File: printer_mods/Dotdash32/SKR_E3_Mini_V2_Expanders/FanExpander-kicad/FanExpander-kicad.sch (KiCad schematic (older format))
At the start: 66 parts, among them J0 FAN0, J1 FAN1, J10 FAN0_IN, J11 HI_PWR_Inputs, J2 FAN2, J3 FAN3, J4 FAN4, J5 FAN5, J6 FAN6, J7 FAN7, J8 EXP1_IN, J9 5V_In, Q1 IRLML6344, Q2 IRLML6344, Q3 IRLML6344, Q4 IRLML6344, Q5 IRLML6344, Q6 IRLML6344, Q7 IRLML6344

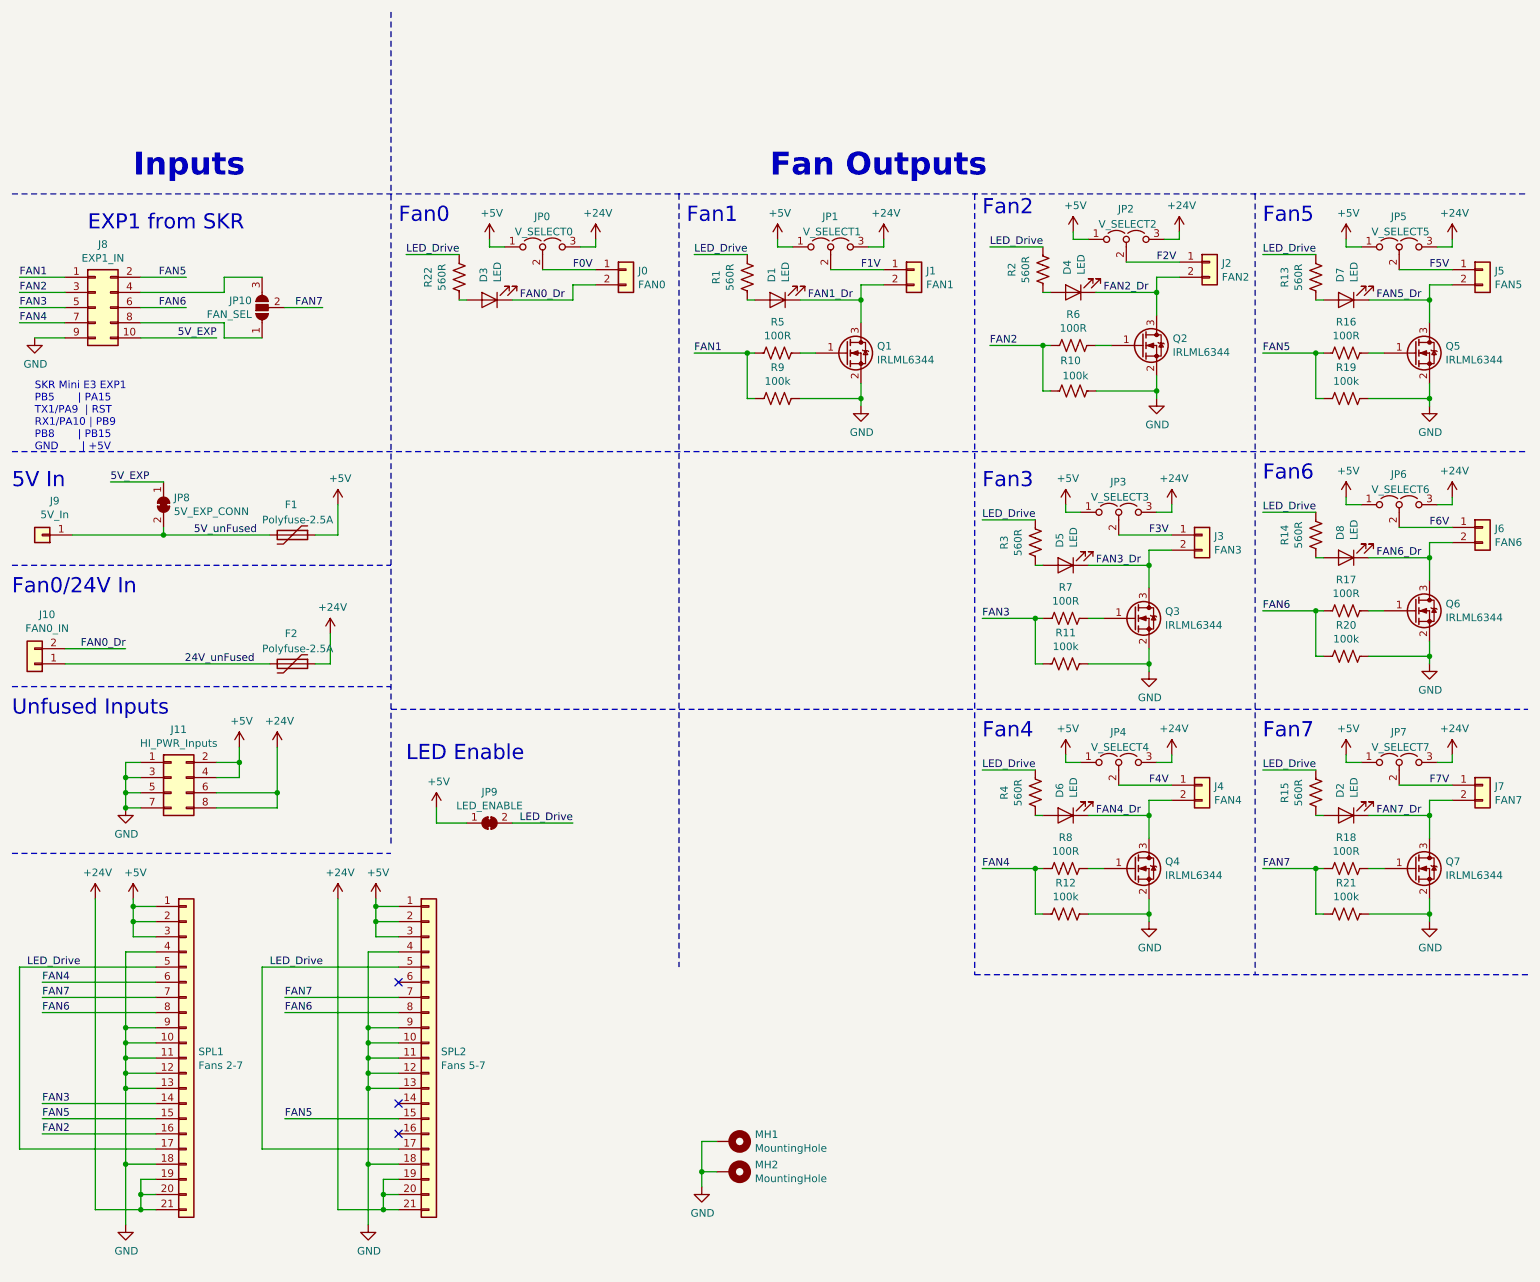
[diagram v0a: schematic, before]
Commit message: feat: move SMD components to bottom for sizing
this really messes with the designator cleanliness, but alas,
sacrifices must be made.  It's really smalll now!

Also some schematic cleaning.  Should there be a second set of
mounting holes next to the connector?  unclear...
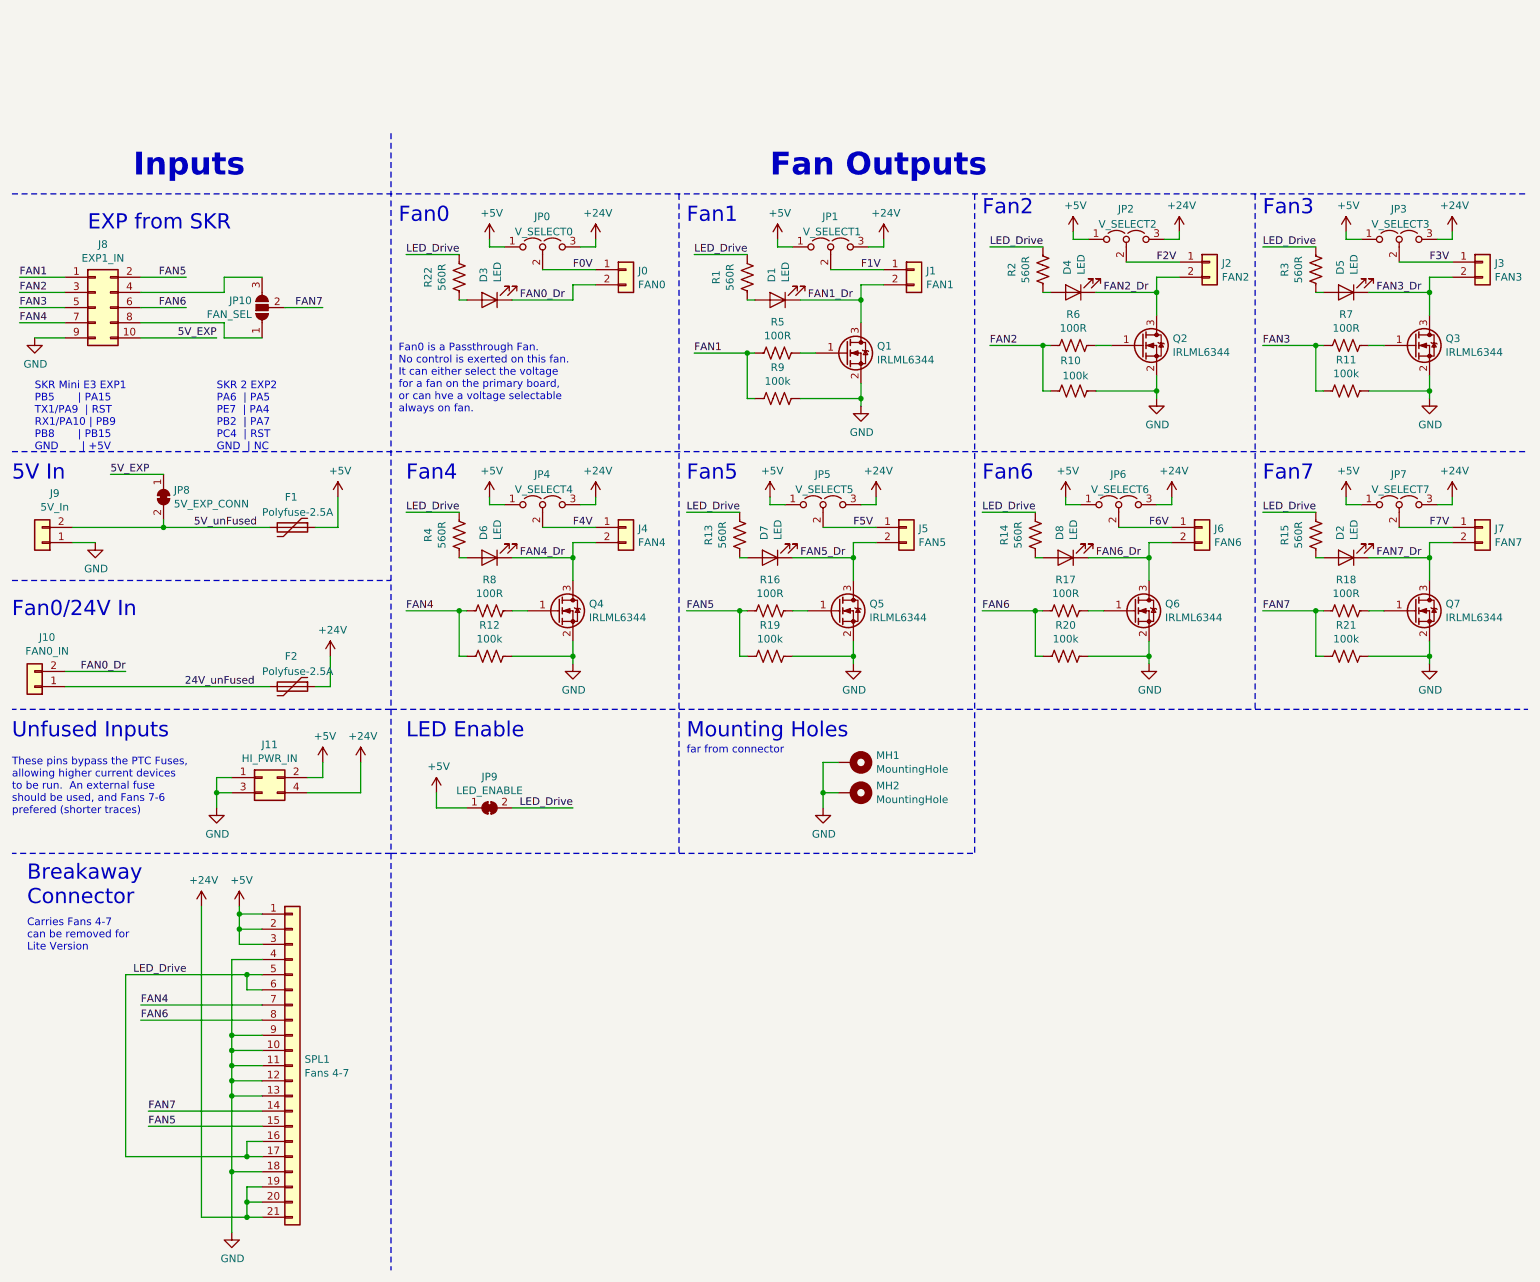
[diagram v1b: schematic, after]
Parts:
- removed J11: HI_PWR_Inputs, Pin_Headers:Pin_Header_Straight_2x04_Pitch2.54mm, symbol Connector_Generic:Conn_02x04_Odd_Even
- removed J9: 5V_In, Pin_Headers:Pin_Header_Straight_1x01_Pitch2.54mm, symbol Connector_Generic:Conn_01x01
- removed SPL2: Fans 5-7, Pin_Headers:Pin_Header_Straight_1x21_Pitch1.00mm, symbol Connector_Generic:Conn_01x21
- added J11: HI_PWR_IN, Pin_Headers:Pin_Header_Straight_2x02_Pitch2.54mm, symbol Connector_Generic:Conn_02x02_Odd_Even
- added J9: 5V_In, Pin_Headers:Pin_Header_Straight_1x02_Pitch2.54mm, symbol Connector_Generic:Conn_01x02
- D1, D2, D3, D4, D5, D6, D7, D8: footprint LEDs:LED_0603_HandSoldering -> LED_SMD:LED_1206_3216Metric_ReverseMount_Hole1.8x2.4mm
- MH1, MH2: footprint Mounting_Holes:MountingHole_3.2mm_M3 -> Mounting_Holes:MountingHole_3.2mm_M3_Pad
- R1, R10, R11, R12, R13, R14, R15, R16, R17, R18, R19, R2, R20, R21, R22, R3, R4, R5, R6, R7, R8, R9: footprint Resistors_SMD:R_0603_HandSoldering -> Resistors_SMD:R_0603
- SPL1: value Fans 2-7 -> Fans 4-7
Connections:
- net +24V: now also J11.4 (Pin_4)
- net +5V: now also J11.2 (Pin_2)
- net 5V_unFused: now also J9.2 (Pin_2)
- net FAN2: no longer SPL1.16 (Pin_16)
- net FAN3: no longer SPL1.14 (Pin_14)
- net FAN4: now also SPL1.7 (Pin_7); no longer SPL1.6 (Pin_6)
- net FAN7: now also SPL1.14 (Pin_14); no longer SPL1.7 (Pin_7)
- net GND: now also J11.1 (Pin_1), J11.3 (Pin_3), J9.1 (Pin_1)
- net LED_Drive: now also SPL1.16 (Pin_16), SPL1.6 (Pin_6)
- no-connect marks 3 -> 0
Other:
- note added: "Breakaway\nConnector"
- note added: "Carries Fans 4-7\ncan be removed for \nLite Version"
- note added: "EXP from SKR"
- note added: "Fan0 is a Passthrough Fan.\nNo control is exerted on this fan.\nIt can either select the voltage \nfor a fan on the primary board,\nor can hve a voltage selectable \nalways on fan."
- note added: "Mounting Holes"
- note added: "SKR 2 EXP2\nPA6 | PA5\nPE7 | PA4\nPB2 | PA7\nPC4 | RST\nGND | NC"
- note added: "These pins bypass the PTC Fuses,\nallowing higher current devices\nto be run. An external fuse \nshould be used, and Fans 7-6\nprefered (shorter traces)"
- note added: "far from connector"
- note removed: "EXP1 from SKR"
- moved on the sheet: D2, D5, D6, D7, D8, F1, F2, J10, J3, J4, J5, J6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
